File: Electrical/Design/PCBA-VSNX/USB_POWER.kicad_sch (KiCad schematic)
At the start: 15 parts, among them J601 TYPE-C-32-M-12, U601 C5451661, U602 LN1134A332MR-G

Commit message: SUKU sync
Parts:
- U601: footprint suku_basics:SOT-23-6 -> suku_basics:SOT-23-6-AND-SOT-363
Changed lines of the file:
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@@
 			)
 		)
-		(property "Footprint" "suku_basics:SOT-23-6"
+		(property "Footprint" "suku_basics:SOT-23-6-AND-SOT-363"
 			(at 94.615 39.37 0)
 			(effects

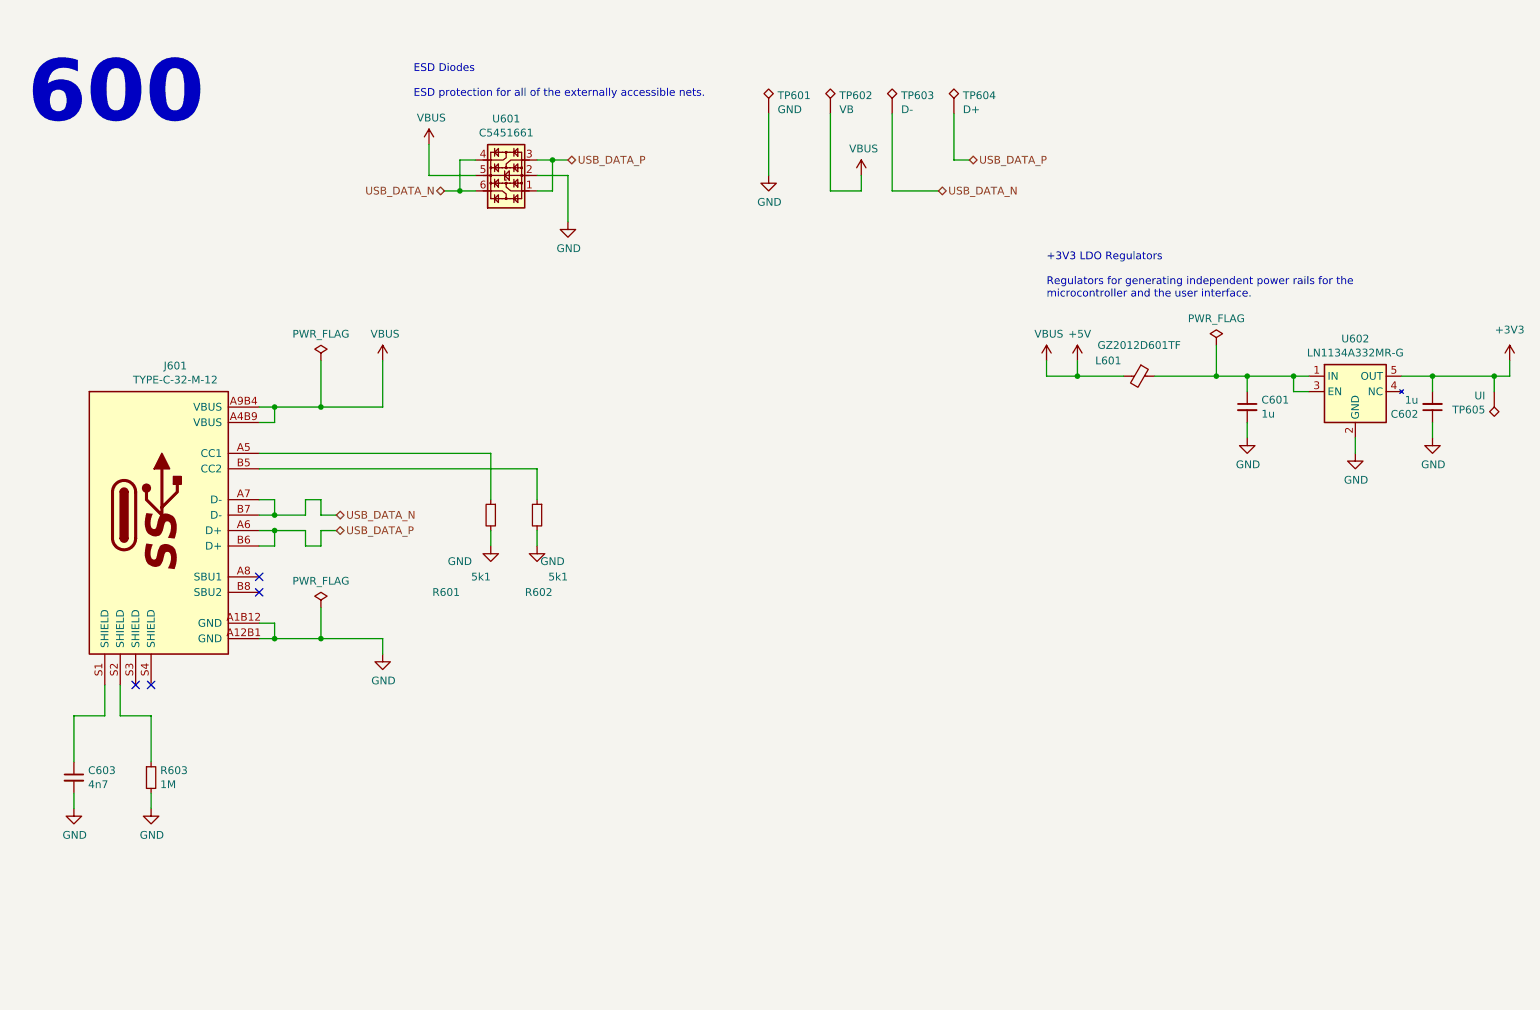
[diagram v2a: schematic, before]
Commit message: SUKU VSNX debug adapter added
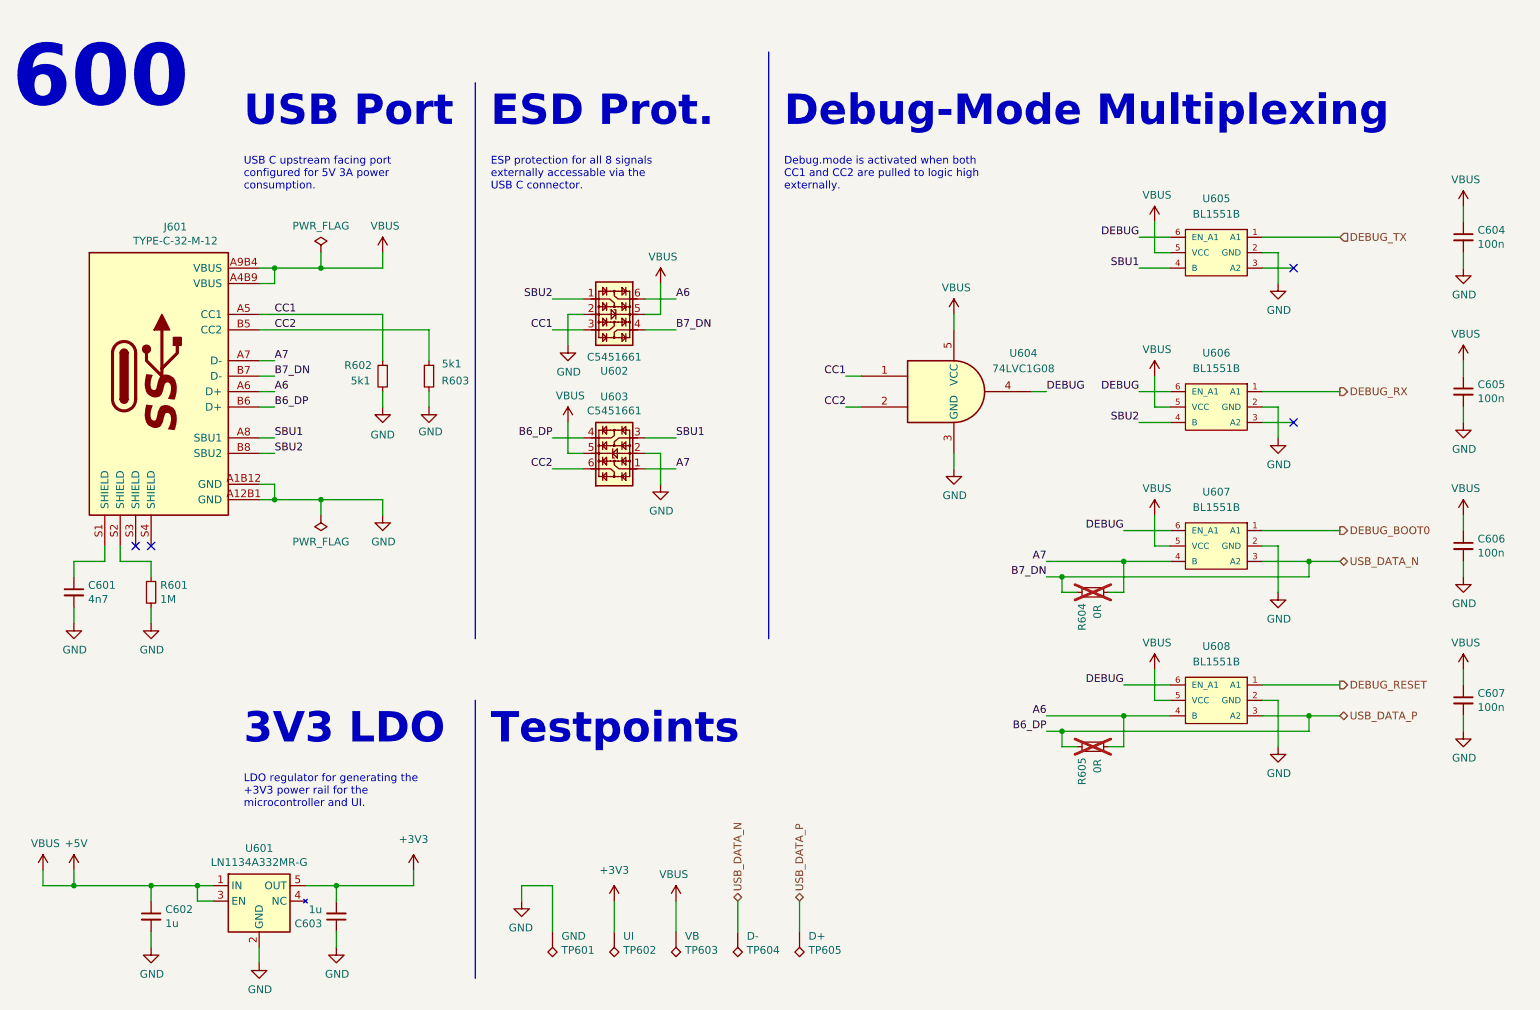
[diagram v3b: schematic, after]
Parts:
- removed L601: GZ2012D601TF, suku_basics:FERRIT_0805, symbol suku_basics:FERRIT
- removed TP605: UI, TestPoint:TestPoint_Pad_D1.0mm, symbol Connector:TestPoint_Alt
- removed U601: C5451661, suku_basics:SOT-23-6-AND-SOT-363, symbol suku_basics:U_ESD_4ch
- added C604, C605, C606, C607: 100n, suku_basics:CAP_0402, symbol suku_basics:CAP
- added R604, R605: 0R, suku_basics:RES_0402, symbol suku_basics:RES
- added TP602: UI, TestPoint:TestPoint_Pad_D1.0mm, symbol Connector:TestPoint_Alt
- added U602, U603: C5451661, suku_basics:SOT-23-6, symbol suku_basics:U_ESD_4ch
- added U604: 74LVC1G08, suku_basics:SOT-23-5-AND-TSSOP5, symbol 74xGxx:74LVC1G08
- added U605, U606, U607, U608: BL1551B, suku_basics:SOT-363_SC-70-6, symbol suku_basics:BL1551B
- renumbered C603 to C601, C601 to C602, C602 to C603, R603 to R601, R601 to R602, R602 to R603, TP602 to TP603, TP603 to TP604, TP604 to TP605, U602 to U601
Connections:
- net +3V3: now also TP602.1
- net +5V: now also C602.1, U601.1 (IN), U601.3 (EN), C604.1, C605.1, C606.1, C607.1, U602.5, U603.5, U604.5 (VCC), U605.5 (VCC), U606.5 (VCC), U607.5 (VCC), U608.5 (VCC)
- net GND: now also C604.2, C605.2, C606.2, C607.2, U602.2, U603.2, U604.3 (GND), U605.2 (GND), U606.2 (GND), U607.2 (GND), U608.2 (GND)
- net USB_DATA_N: now also R604.1, U602.4, U607.3 (A2); no longer J601.A7 (D-)
- net USB_DATA_P: now also R605.1, U603.4, U608.3 (A2); no longer J601.A6 (D+)
- net CC2: now reaches J601.B5 (CC2), R603.1
- net CC2: now also U603.6, U604.2
- net CC1: now reaches J601.A5 (CC1), R602.1
- net CC1: now also U602.3, U604.1
- net SBU1: now reaches J601.A8 (SBU1)
- net SBU1: now also U603.3, U605.4 (B)
- net SBU2: now reaches J601.B8 (SBU2)
- net SBU2: now also U602.1, U606.4 (B)
- new net A6: J601.A6 (D+), R605.2, U602.6, U608.4 (B)
- new net A7: J601.A7 (D-), R604.2, U603.1, U607.4 (B)
- new net DEBUG: U604.4, U605.6 (EN_A1), U606.6 (EN_A1), U607.6 (EN_A1), U608.6 (EN_A1)
- new net DEBUG_BOOT0: U607.1 (A1)
- new net DEBUG_RESET: U608.1 (A1)
- new net DEBUG_RX: U606.1 (A1)
- new net DEBUG_TX: U605.1 (A1)
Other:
- note added: "3V3 LDO"
- note added: "Debug-Mode Multiplexing"
- note added: "Debug.mode is activated when both CC1 and CC2 are pulled to logic high externally."
- note added: "ESD Prot."
- note added: "ESP protection for all 8 signals externally accessable via the USB C connector."
- note added: "LDO regulator for generating the +3V3 power rail for the microcontroller and UI."
- note added: "Testpoints"
- note added: "USB C upstream facing port configured for 5V 3A power consumption."
- note added: "USB Port"
- note removed: "+3V3 LDO Regulators Regulators for generating independent power rails for the microcontroller and the user interface."
- note removed: "ESD Diodes ESD protection for all of the externally accessible nets."
- moved on the sheet: C601, C602, C603, J601, R601, R602, R603, TP601, TP603, TP604, TP605, U601
